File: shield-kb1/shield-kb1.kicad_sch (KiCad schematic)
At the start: 13 parts, among them J1 LEFT, J2 RIGHT, SW1 SW_SPST, SW2 SW_SPST, SW3 SW_SPST, SW4 SW_SPST

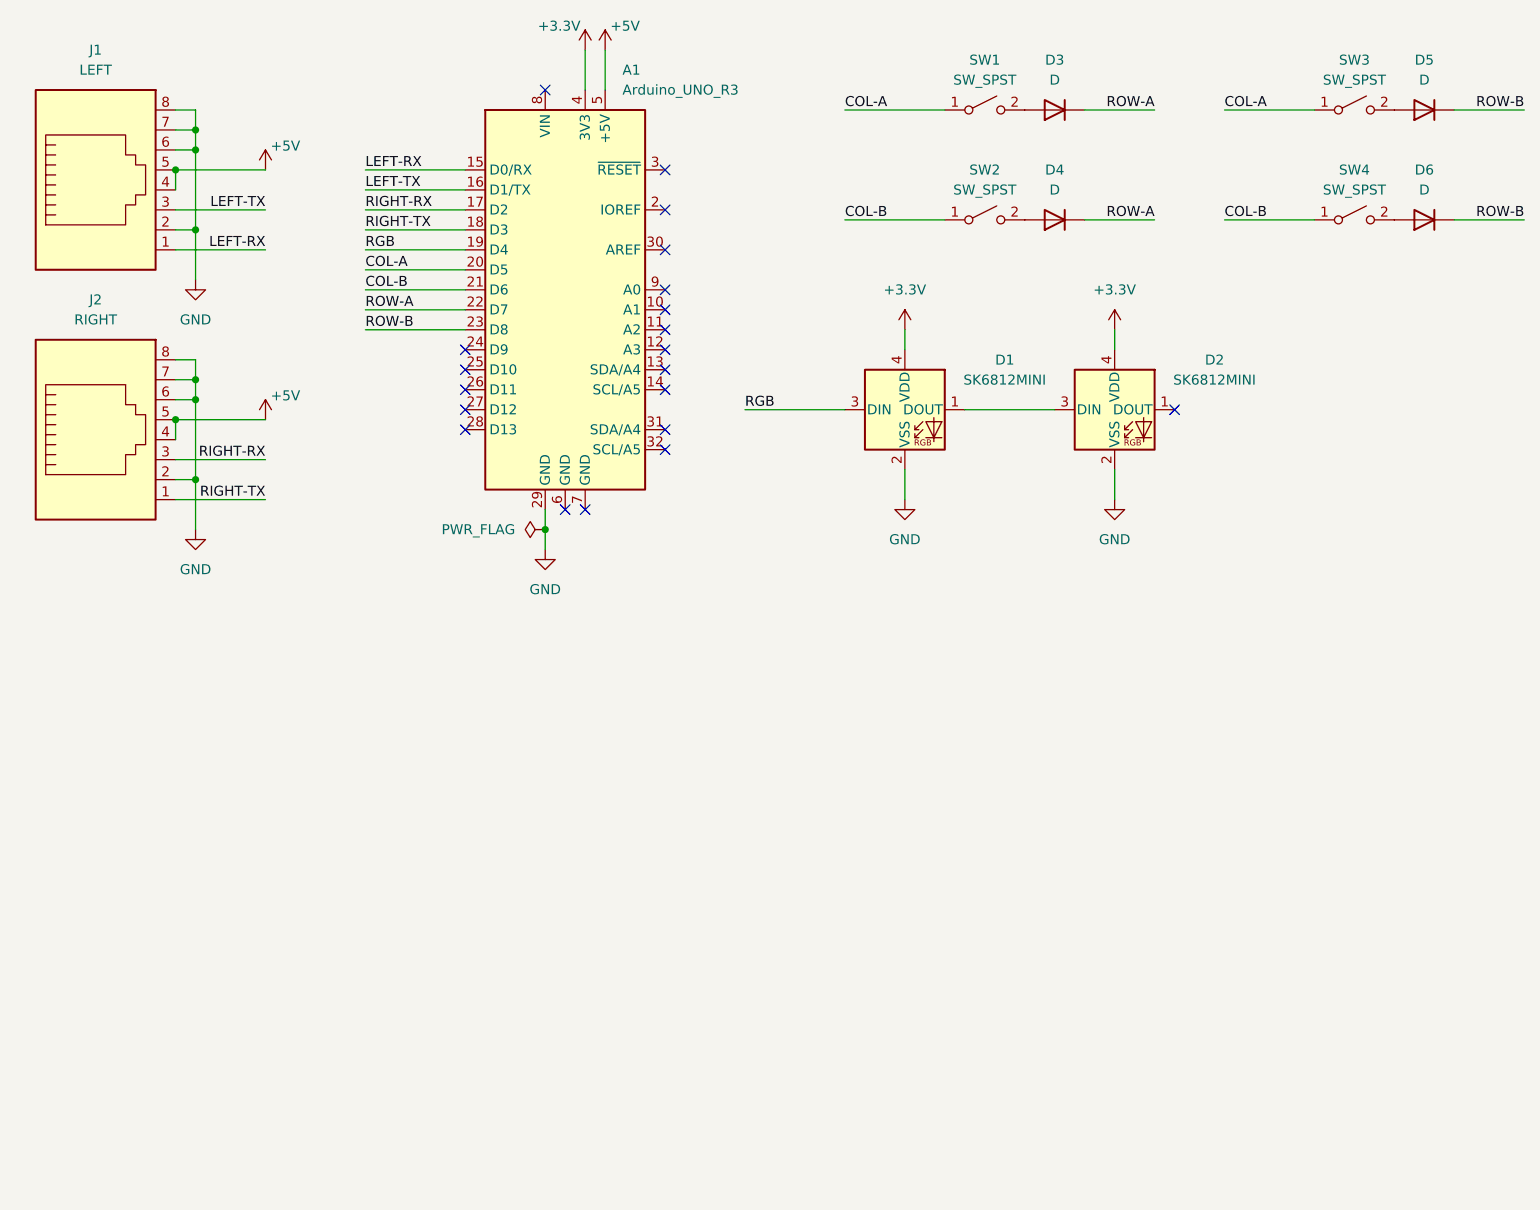
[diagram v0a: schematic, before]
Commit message: shield-kb1: rev-b updates: LEDs
In addition to actually hooking up the switches, add a PWM RGB LED. It
is hard to find these that will work with 3.2V, hopefully this one will.
It is fairly small, and I've come up with some resistors for about 15mA.

I've also added a jumper to allow the SK6812 to be powered either from
3.3V or 5V, which should help figring out issues with that.
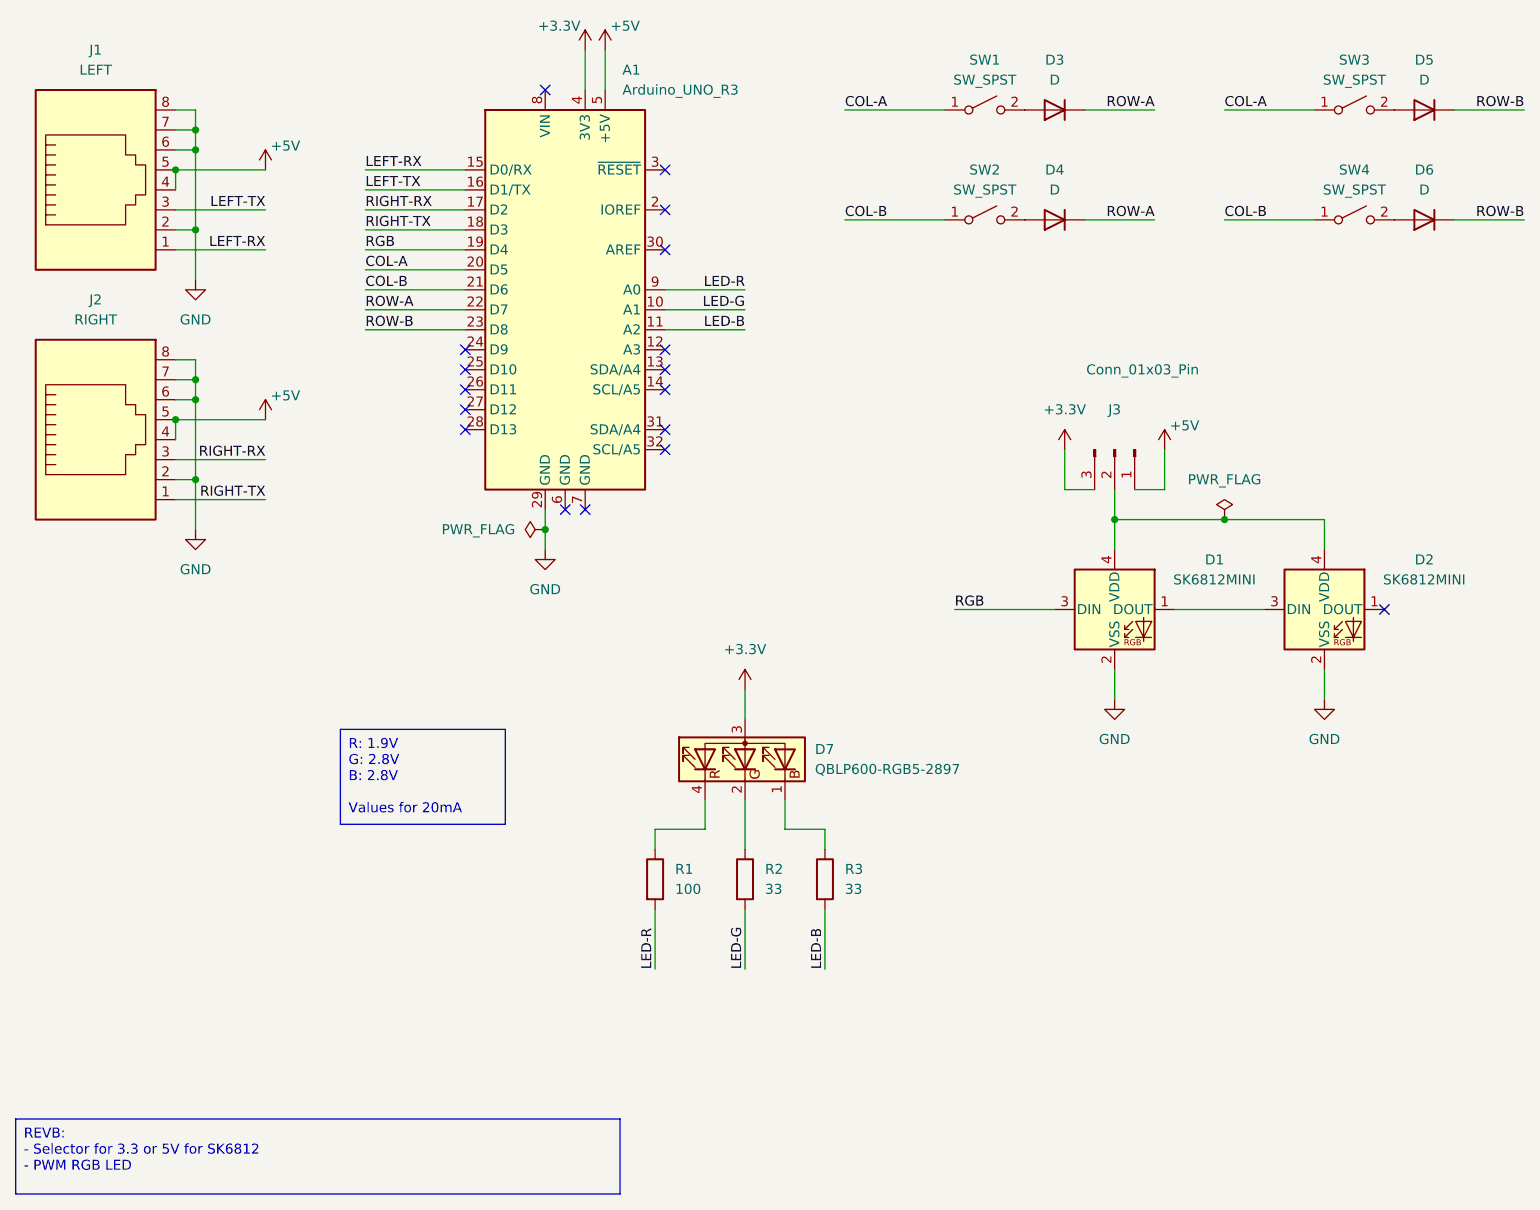
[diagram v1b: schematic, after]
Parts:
- added D7: QBLP600-RGB5-2897, davidb-keyboard-foot:QBLP600-RGB5-2897, symbol Device:LED_BGAR
- added J3: Conn_01x03_Pin, Connector_PinHeader_2.54mm:PinHeader_1x03_P2.54mm_Vertical, symbol Connector:Conn_01x03_Pin
- added R1: 100, Resistor_SMD:R_0603_1608Metric_Pad0.98x0.95mm_HandSolder, symbol Device:R
- added R2, R3: 33, Resistor_SMD:R_0603_1608Metric_Pad0.98x0.95mm_HandSolder, symbol Device:R
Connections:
- net +3.3V: now also D7.3 (A), J3.3 (Pin_3); no longer D1.4 (VDD), D2.4 (VDD)
- net +5V: now also J3.1 (Pin_1)
- net LED-G: now reaches A1.10 (A1)
- net LED-G: now also R2.2
- net LED-B: now reaches A1.11 (A2)
- net LED-B: now also R3.2
- net LED-R: now reaches A1.9 (A0)
- net LED-R: now also R1.2
- new net: D7.2 (GK), R2.1
- new net: D1.4 (VDD), D2.4 (VDD), J3.2 (Pin_2)
- new net: D7.1 (BK), R3.1
- new net: D7.4 (RK), R1.1
- no-connect marks 20 -> 17
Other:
- moved on the sheet: D1, D2
